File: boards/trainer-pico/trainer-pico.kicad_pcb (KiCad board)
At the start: 2 copper layers, 132.1 x 99.1 mm, 18 parts, among them J1 Conn_01x08_Pin, J10 Conn_01x04_Socket, J11 Conn_01x17_Pin, J12 Conn_01x17_Socket, J13 Conn_01x17_Socket, J14 Conn_01x17_Pin, J2 Conn_01x04_Pin, J3 Conn_01x06_Pin, J4 Conn_01x04_Pin, J5 Conn_01x04_Pin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

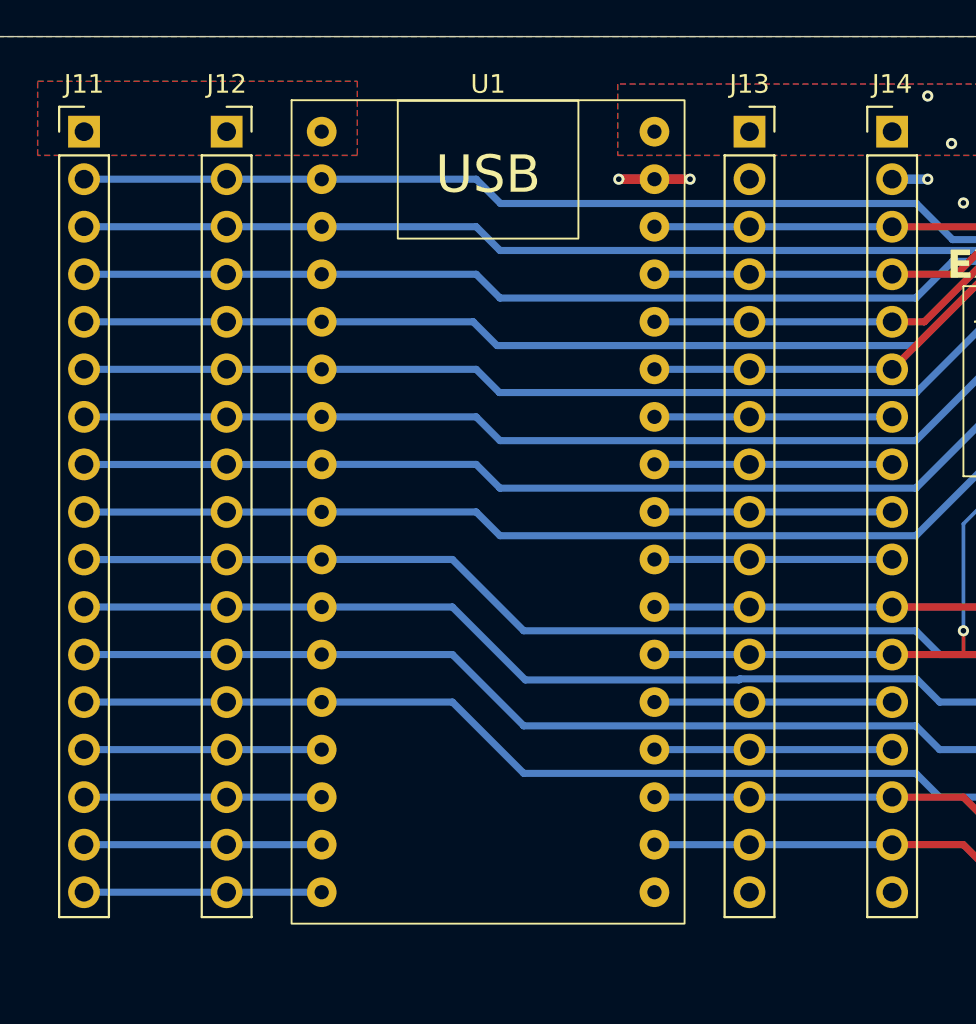
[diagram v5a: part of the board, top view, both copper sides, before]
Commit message: Pico の両側に IO 番号の刻印を追加
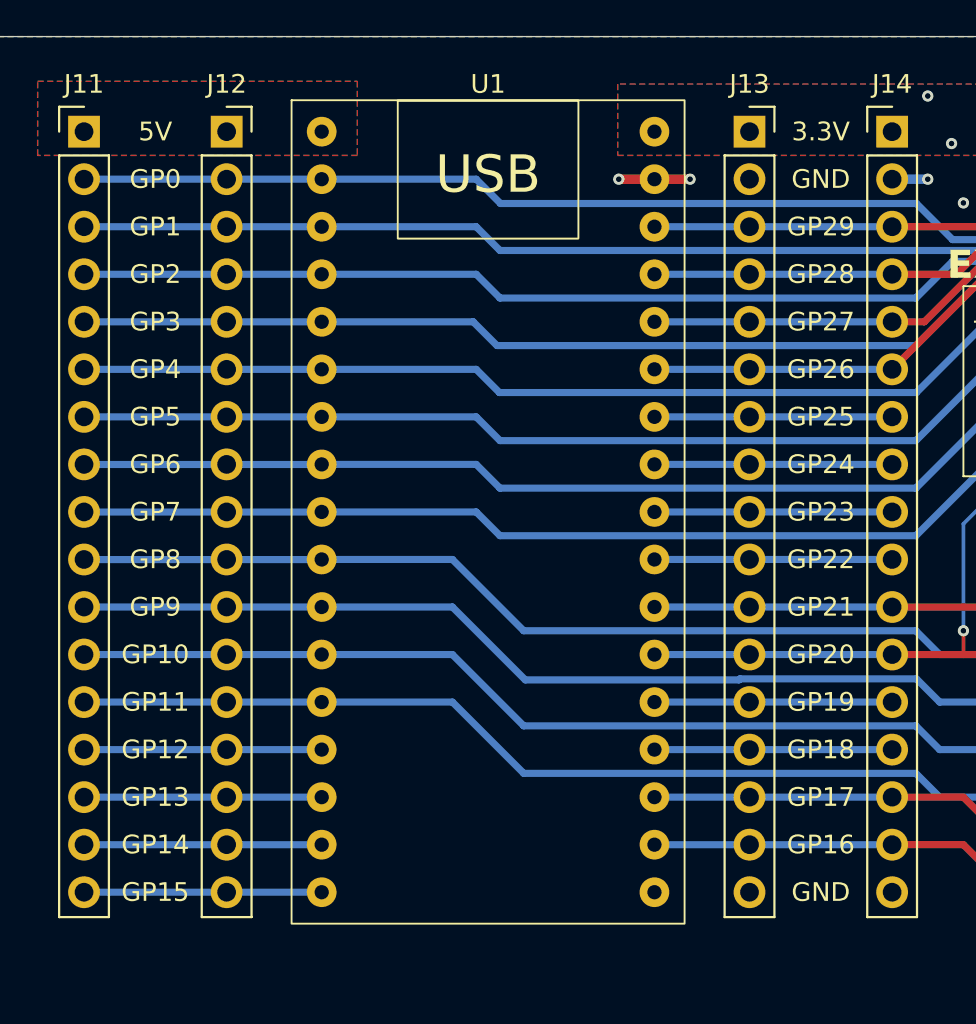
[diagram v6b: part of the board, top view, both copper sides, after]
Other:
- board text added: "5V"
- board text added: "GP10"
- board text added: "GP11"
- board text added: "GP12"
- board text added: "GP13"
- board text added: "GP14"
- board text added: "GP15"
- board text added: "GP16"
- board text added: "GP17"
- board text added: "GP18"
- board text added: "GP19"
- board text added: "GP20"
- board text added: "GP21"
- board text added: "GP22"
- board text added: "GP23"
- board text added: "GP24"
- board text added: "GP25"
- board text added: "GP26"
- board text added: "GP27"
- board text added: "GP28"
- board text added: "GP29"
- board text added: "GP8"
- board text added: "GP9"

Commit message: 配線を微修正
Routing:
- net GND: track 5.72 -> 13.5 mm
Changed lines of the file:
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@@
+	)
+	(segment
+		(start 76.835 66.04)
+		(end 78.105 67.31)
+		(width 0.381)
+		(layer "B.Cu")
+		(net 3)
+	)
+	(segment
+		(start 68.58 66.04)
+		(end 76.835 66.04)
+		(width 0.381)
+		(layer "B.Cu")
+		(net 3)
+	)
+	(segment
+		(start 78.105 67.31)
+		(end 100.33 67.31)
+		(width 0.381)
+		(layer "B.Cu")
+		(net 3)
 	)
 	(segment
@@
 	)
 	(segment
-		(start 76.835 66.04)
-		(end 78.0755 67.2805)
+		(start 136.19175 59.38825)
+		(end 139.7 55.88)
 		(width 0.381)
 		(layer "B.Cu")
@@
 	)
 	(segment
-		(start 100.3595 67.2805)
+		(start 106.207 61.433)
+		(end 119.617026 61.433)
+		(width 0.381)
+		(layer "B.Cu")
+		(net 3)
+	)
+	(segment
+		(start 68.58 66.04)
+		(end 55.88 66.04)
+		(width 0.381)
+		(layer "B.Cu")
+		(net 3)
+	)
+	(segment
+		(start 100.33 67.31)
 		(end 106.207 61.433)
-		(width 0.381)
-		(layer "B.Cu")
-		(net 3)
-	)
-	(segment
-		(start 68.58 66.04)
-		(end 76.835 66.04)
 		(width 0.381)
 		(layer "B.Cu")
@@
 	)
 	(segment
-		(start 78.0755 67.2805)
-		(end 100.3595 67.2805)
-		(width 0.381)
-		(layer "B.Cu")
-		(net 3)
-	)
-	(segment
-		(start 68.58 66.04)
-		(end 55.88 66.04)
-		(width 0.381)
-		(layer "B.Cu")
-		(net 3)
-	)
-	(segment
-		(start 106.207 61.433)
-		(end 119.617026 61.433)
-		(width 0.381)
-		(layer "B.Cu")
-		(net 3)
-	)
-	(segment
-		(start 136.19175 59.38825)
-		(end 139.7 55.88)
-		(width 0.381)
-		(layer "B.Cu")
-		(net 3)
-	)
-	(segment
 		(start 144.78 55.88)
 		(end 144.78 63.5)
@@
 	)
 	(segment
-		(start 100.3595 57.1795)
-		(end 78.1345 57.1795)
-		(width 0.381)
-		(layer "B.Cu")
-		(net 8)
-	)
-	(segment
 		(start 118.654394 59.109)
 		(end 102.289 59.109)
@@
 	)
 	(segment
+		(start 78.105 57.15)
+		(end 76.835 55.88)
+		(width 0.381)
+		(layer "B.Cu")
+		(net 8)
+	)
+	(segment
 		(start 55.88 55.88)
 		(end 68.58 55.88)
@@
 	)
 	(segment
-		(start 102.289 59.109)
-		(end 100.3595 57.1795)
-		(width 0.381)
-		(layer "B.Cu")
-		(net 8)
-	)
-	(segment
 		(start 120.699144 57.06425)
 		(end 118.654394 59.109)
@@
 	)
 	(segment
+		(start 102.289 59.109)
+		(end 100.33 57.15)
+		(width 0.381)
+		(layer "B.Cu")
+		(net 8)
+	)
+	(segment
 		(start 76.835 55.88)
 		(end 68.58 55.88)
@@
 	)
 	(segment
-		(start 78.1345 57.1795)
-		(end 76.835 55.88)
-		(width 0.381)
-		(layer "B.Cu")
-		(net 8)
-	)
-	(segment
 		(start 129.54 55.88)
 		(end 128.35575 57.06425)
@@
 	)
 	(segment
+		(start 100.33 57.15)
+		(end 78.105 57.15)
+		(width 0.381)
+		(layer "B.Cu")
+		(net 8)
+	)
+	(segment
 		(start 165.1 55.88)
 		(end 158.804 49.584)
@@
 		(layer "B.Cu")
 		(net 12)
+	)
+	(segment
+		(start 92.71 57.15)
+		(end 91.44 55.88)
+		(width 0.508)
+		(layer "F.Cu")
+		(net 13)
+	)
+	(segment
+		(start 91.44 55.88)
+		(end 90.17 57.15)
+		(width 0.508)
+		(layer "F.Cu")
+		(net 13)
+	)
+	(segment
+		(start 99.06 55.88)
+		(end 100.33 57.15)
+		(width 0.508)
+		(layer "F.Cu")
+		(net 13)
+	)
+	(segment
+		(start 99.06 55.88)
+		(end 97.79 57.15)
+		(width 0.508)
+		(layer "F.Cu")
+		(net 13)
 	)
 	(segment
@@
 	)
 	(via
-		(at 100.965 55.88)
+		(at 101.6 55.88)
 		(size 0.6)
 		(drill 0.3)
@@
 	)
 	(segment
-		(start 100.965 55.88)
+		(start 101.6 55.88)
 		(end 99.06 55.88)
 		(width 0.508)
@@
 	)
 	(segment
-		(start 75.565 78.74)
-		(end 79.46075 82.63575)
-		(width 0.381)
-		(layer "B.Cu")
-		(net 14)
-	)
-	(segment
 		(start 68.58 78.74)
 		(end 55.88 78.74)
@@
 	)
 	(segment
-		(start 90.926168 82.5795)
+		(start 79.4045 82.5795)
 		(end 100.3595 82.5795)
 		(width 0.381)
@@
 	)
 	(segment
-		(start 90.869918 82.63575)
-		(end 90.926168 82.5795)
+		(start 100.3595 82.5795)
+		(end 101.6 83.82)
+		(width 0.381)
+		(layer "B.Cu")
+		(net 14)
+	)
+	(segment
+		(start 68.58 78.74)
+		(end 75.565 78.74)
+		(width 0.381)
+		(layer "B.Cu")
+		(net 14)
+	)
+	(segment
+		(start 75.565 78.74)
+		(end 79.4045 82.5795)
 		(width 0.381)
 		(layer "B.Cu")
@@
 	)
 	(segment
-		(start 75.565 78.74)
-		(end 68.58 78.74)
-		(width 0.381)
-		(layer "B.Cu")
-		(net 14)
-	)
-	(segment
-		(start 79.46075 82.63575)
-		(end 90.869918 82.63575)
-		(width 0.381)
-		(layer "B.Cu")
-		(net 14)
-	)
-	(segment
-		(start 100.3595 82.5795)
-		(end 101.6 83.82)
-		(width 0.381)
-		(layer "B.Cu")
-		(net 14)
-	)
-	(segment
 		(start 111.76 86.36)
 		(end 119.38 86.36)
@@
 	)
 	(segment
+		(start 109.855 67.945)
+		(end 109.22 67.945)
+		(width 0.2)
+		(layer "F.Cu")
+		(net 18)
+	)
+	(segment
+		(start 110.49 67.31)
+		(end 109.855 67.945)
+		(width 0.2)
+		(layer "F.Cu")
+		(net 18)
+	)
+	(segment
 		(start 110.935 67.31)
-		(end 109.855 67.31)
-		(width 0.2)
-		(layer "F.Cu")
-		(net 18)
-	)
-	(segment
-		(start 109.855 67.31)
-		(end 109.22 67.945)
+		(end 110.49 67.31)
 		(width 0.2)
 		(layer "F.Cu")
@@
 	)
 	(segment
+		(start 109.855 69.215)
+		(end 109.22 69.215)
+		(width 0.2)
+		(layer "F.Cu")
+		(net 19)
+	)
+	(segment
 		(start 111.76 104.14)
 		(end 109.22 104.14)
@@
 	)
 	(segment
-		(start 109.855 69.85)
-		(end 109.22 69.215)
+		(start 110.935 69.85)
+		(end 110.49 69.85)
+		(width 0.2)
+		(layer "F.Cu")
+		(net 19)
+	)
+	(segment
+		(start 110.49 69.85)
+		(end 109.855 69.215)
 		(width 0.2)
 		(layer "F.Cu")
@@
 		(layer "F.Cu")
 		(net 19)
-	)
-	(segment
-		(start 110.935 69.85)
-		(end 109.855 69.85)
-		(width 0.2)
-		(layer "F.Cu")
-		(net 19)

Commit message: 外部電源追加
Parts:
- added C1: 100uF, Capacitor_THT:CP_Radial_D8.0mm_P3.50mm, F.Cu at (64.8, 112.9)
- added C2: 100uF, Capacitor_THT:CP_Radial_D8.0mm_P3.50mm, F.Cu at (64.8, 134.2)
- added C3: 0.22uF, Capacitor_SMD:C_0805_2012Metric, F.Cu at (71.1, 111.3)
- added C4: 0.22uF, Capacitor_SMD:C_0805_2012Metric, F.Cu at (71.1, 132.6)
- added C5: 0.1uF, Capacitor_SMD:C_0603_1608Metric, F.Cu at (86.4, 111.3)
- added C6: 0.1uF, Capacitor_SMD:C_0603_1608Metric, F.Cu at (86.4, 132.6)
- added C7: 47uF, Capacitor_THT:CP_Radial_D6.3mm_P2.50mm, F.Cu at (91.4, 112.4)
- added C8: 47uF, Capacitor_THT:CP_Radial_D6.3mm_P2.50mm, F.Cu at (91.4, 133.8)
- added C9: 10uF, Capacitor_SMD:C_1206_3216Metric, F.Cu at (50.0, 57.1)
- added D1: D, Diode_SMD:D_SOD-123F, F.Cu at (78.7, 119.6)
- added D2: D, Diode_SMD:D_SOD-123F, F.Cu at (78.7, 141.0)
- added D3: D, Diode_SMD:D_SOD-123F, F.Cu at (51.6, 62.0)
- added J15: Barrel_Jack_Switch, Connector_BarrelJack:BarrelJack_Horizontal, F.Cu at (55.9, 106.7)
- added J16: Conn_01x04_Pin, Connector_PinHeader_2.54mm:PinHeader_1x04_P2.54mm_Vertical, F.Cu at (128.3, 142.2)
- added J17: Conn_01x04_Pin, Connector_PinHeader_2.54mm:PinHeader_1x04_P2.54mm_Vertical, F.Cu at (143.5, 142.2)
- added J18: Conn_01x04_Pin, Connector_PinHeader_2.54mm:PinHeader_1x04_P2.54mm_Vertical, F.Cu at (158.8, 142.2)
- added J19: Conn_01x08_Pin, Connector_PinHeader_2.54mm:PinHeader_1x08_P2.54mm_Vertical, F.Cu at (174.0, 78.7)
- added J20: Conn_01x08_Pin, Connector_PinHeader_2.54mm:PinHeader_1x08_P2.54mm_Vertical, F.Cu at (174.0, 111.8)
- added U2: L7805, Package_TO_SOT_SMD:TO-263-2, F.Cu at (78.7, 107.6)
- added U3: L7809, Package_TO_SOT_SMD:TO-263-2, F.Cu at (78.7, 128.9)
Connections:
- net +5V renamed VBUS
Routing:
- net GND: track 13.5 -> 36.0 mm
- net +12V: track 0.00 -> 9.74 mm
- net +9V: track 0.00 -> 4.87 mm
- net +5V: track 0.00 -> 4.86 mm
- net VBUS: track 0.00 -> 3.45 mm
- added copper zone on F.Cu, net +12V
- added copper zone on F.Cu, net +5V
- added copper zone on F.Cu, net +9V
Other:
- board text added: "12V"
- board text added: "9V"
- board text added: "EXT POWER SOURCE"
